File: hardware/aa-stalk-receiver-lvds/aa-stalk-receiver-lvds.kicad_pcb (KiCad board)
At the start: 2 copper layers, 67.3 x 50.8 mm, 81 parts, among them CN1 Conn_01x02, CN10 Conn_01x03, CN2 Conn_01x04, CN3 6P6C, CN4 Conn_01x03, CN5 Conn_01x02, CN6 Conn_01x02, CN7 Conn_01x02, CN8 Conn_01x02, CN9 Conn_01x03, Q1 KST10, Q2 MCH3484, Q3 MCH3484, U1 AZ1117-5.0, U2 MIC5504-3.3YM5, U3 LM4562, U4 FIN1028, U5 MC3486N

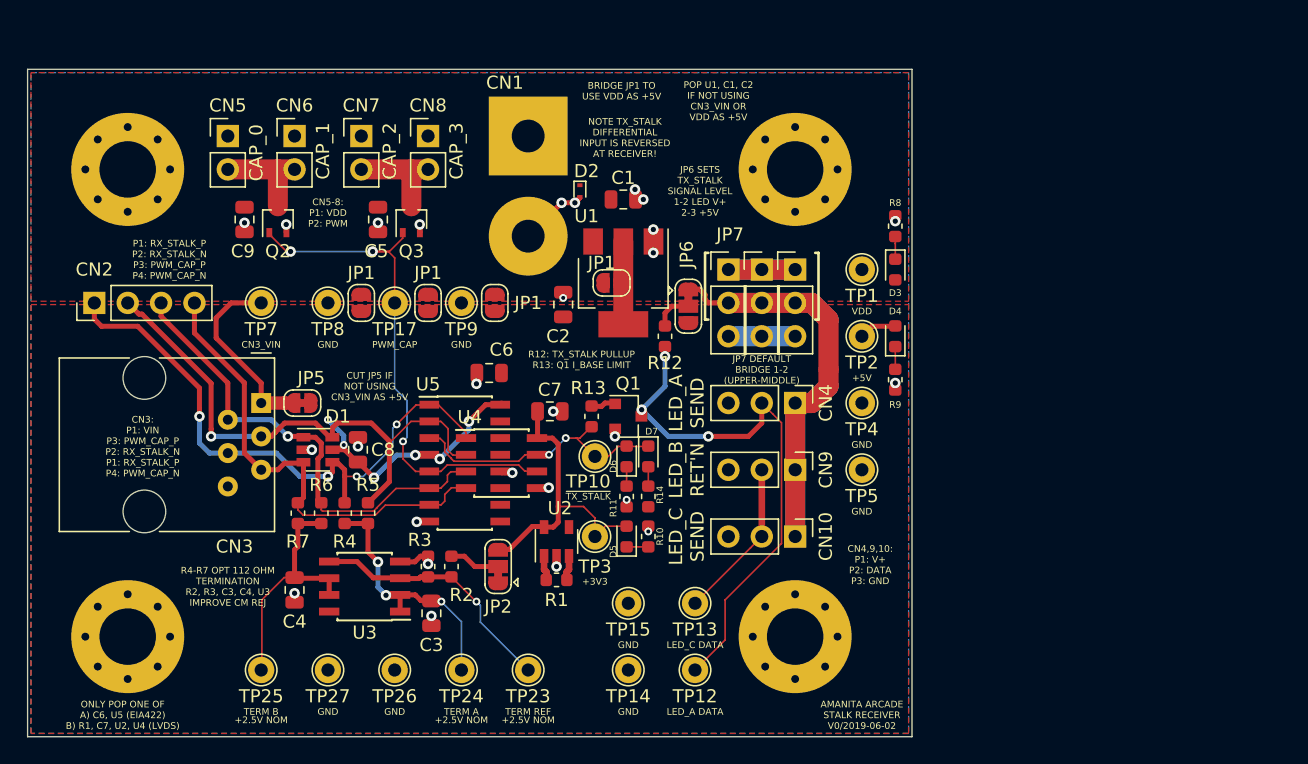
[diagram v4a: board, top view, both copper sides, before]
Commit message: Substantial rework of system, new layouts done for daughterboard, power, stalk receiver
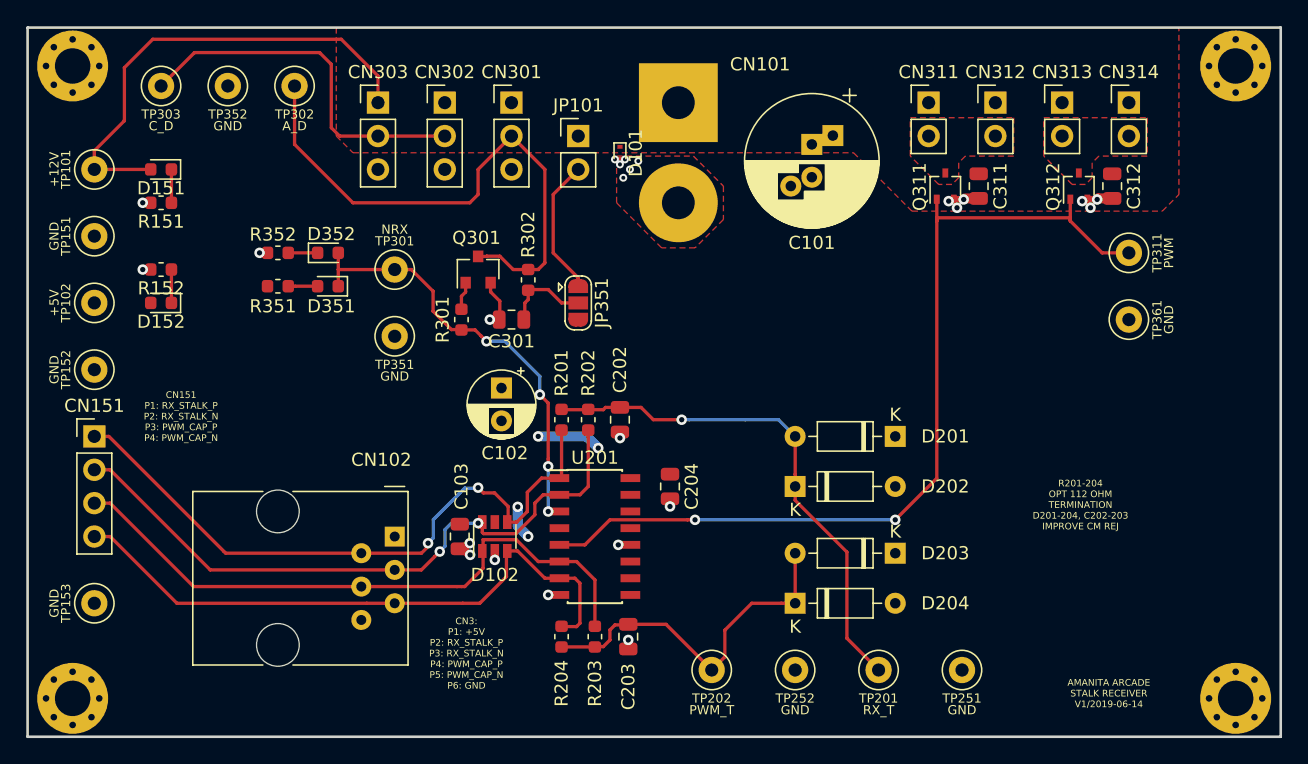
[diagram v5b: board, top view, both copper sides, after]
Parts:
- removed C1, C2, C5, C9: 10u, Capacitor_SMD:C_0805_2012Metric
- removed C3, C4, C7: 0.1u, Capacitor_SMD:C_0805_2012Metric
- removed C6, C8: 1u, Capacitor_SMD:C_0805_2012Metric
- removed CN1: Conn_01x02, Connector_Wire:SolderWirePad_1x02_P7.62mm_Drill2.5mm
- removed CN10, CN4, CN9: Conn_01x03, Connector_PinHeader_2.54mm:PinHeader_1x03_P2.54mm_Vertical
- removed CN2: Conn_01x04, Connector_PinHeader_2.54mm:PinHeader_1x04_P2.54mm_Vertical
- removed CN3: 6P6C, aa-shared:6P6C_Assmann_A-2014-1-4
- removed CN5, CN6, CN7, CN8: Conn_01x02, Connector_PinHeader_2.54mm:PinHeader_1x02_P2.54mm_Vertical
- removed D1: D5V0P4UR6SO, Package_TO_SOT_SMD:SOT-23-6
- removed D2: D_Zener, aa-shared:D_SOD-923
- removed D3, D4, D5, D6, D7: LED, Diode_SMD:D_0603_1608Metric
- removed JP1 (x4): SolderJumper_2_Open, Jumper:SolderJumper-2_P1.3mm_Open_RoundedPad1.0x1.5mm
- removed JP2, JP6: SolderJumper_3_Bridged12, Jumper:SolderJumper-3_P1.3mm_Bridged12_RoundedPad1.0x1.5mm
- removed JP5: SolderJumper_2_Bridged, Jumper:SolderJumper-2_P1.3mm_Bridged_RoundedPad1.0x1.5mm
- removed JP7 (x3): Jumper_3_Bridged12, Connector_PinHeader_2.54mm:PinHeader_1x03_P2.54mm_Vertical
- removed Q1: KST10, Package_TO_SOT_SMD:SOT-23
- removed Q2, Q3: MCH3484, Package_TO_SOT_SMD:SOT-323_SC-70
- removed R1, R2, R3: 10k, Resistor_SMD:R_0603_1608Metric
- removed R10: 220, Resistor_SMD:R_0603_1608Metric
- removed R11, R14, R9: 470, Resistor_SMD:R_0603_1608Metric
- removed R12, R13: 1k, Resistor_SMD:R_0603_1608Metric
- removed R4, R5, R6, R7: 56, Resistor_SMD:R_0603_1608Metric
- removed R8: 1.5k, Resistor_SMD:R_0603_1608Metric
- removed TP1, TP10, TP12, TP13, TP14, TP15, TP17, TP2, TP23, TP24, TP25, TP26, TP27, TP3, TP4, TP5, TP7, TP8, TP9: TestPoint, TestPoint:TestPoint_THTPad_D2.0mm_Drill1.0mm
- removed U1: AZ1117-5.0, Package_TO_SOT_SMD:SOT-223-3_TabPin2
- removed U2: MIC5504-3.3YM5, Package_TO_SOT_SMD:SOT-23-5
- removed U3: LM4562, Package_SO:SOIC-8_3.9x4.9mm_P1.27mm
- removed U4: FIN1028, Package_SO:SOIC-8_3.9x4.9mm_P1.27mm
- removed U5: MC3486N, Package_SO:SOIC-16_3.9x9.9mm_P1.27mm
- added C101: 100u, Capacitor_THT:CP_Radial_D10.0mm_P2.50mm_P5.00mm, F.Cu at (151.1, 59.1)
- added C102: 10u, Capacitor_THT:CP_Radial_D5.0mm_P2.50mm, F.Cu at (127.5, 77.6)
- added C103: 1u, Capacitor_SMD:C_0805_2012Metric, F.Cu at (124.3, 88.9)
- added C202: 0.1u, Capacitor_SMD:C_0805_2012Metric, F.Cu at (136.5, 80.0)
- added C203: 0.1u, Capacitor_SMD:C_0805_2012Metric, F.Cu at (137.2, 96.5)
- added C204: 1u, Capacitor_SMD:C_0805_2012Metric, F.Cu at (140.3, 85.1)
- added C301: 0.1u, Capacitor_SMD:C_0805_2012Metric, F.Cu at (128.3, 72.4)
- added C311: 10u, Capacitor_SMD:C_0805_2012Metric, F.Cu at (163.8, 62.2)
- added C312: 10u, Capacitor_SMD:C_0805_2012Metric, F.Cu at (174.0, 62.2)
- added CN101: Conn_01x02, Connector_Wire:SolderWirePad_1x02_P7.62mm_Drill2.5mm, F.Cu at (141.0, 55.9)
- added CN102: 6P6C, aa-shared:6P6C_Assmann_A-2014-1-4, F.Cu at (119.4, 88.9)
- added CN151: Conn_01x04, Connector_PinHeader_2.54mm:PinHeader_1x04_P2.54mm_Vertical, F.Cu at (96.5, 81.3)
- added CN301: Conn_01x03, Connector_PinHeader_2.54mm:PinHeader_1x03_P2.54mm_Vertical, F.Cu at (128.3, 55.9)
- added CN302: Conn_01x03, Connector_PinHeader_2.54mm:PinHeader_1x03_P2.54mm_Vertical, F.Cu at (123.2, 55.9)
- added CN303: Conn_01x03, Connector_PinHeader_2.54mm:PinHeader_1x03_P2.54mm_Vertical, F.Cu at (118.1, 55.9)
- added CN311: Conn_01x02, Connector_PinHeader_2.54mm:PinHeader_1x02_P2.54mm_Vertical, F.Cu at (160.0, 55.9)
- added CN312: Conn_01x02, Connector_PinHeader_2.54mm:PinHeader_1x02_P2.54mm_Vertical, F.Cu at (165.1, 55.9)
- added CN313: Conn_01x02, Connector_PinHeader_2.54mm:PinHeader_1x02_P2.54mm_Vertical, F.Cu at (170.2, 55.9)
- added CN314: Conn_01x02, Connector_PinHeader_2.54mm:PinHeader_1x02_P2.54mm_Vertical, F.Cu at (175.3, 55.9)
- added D101: D_Zener, aa-shared:D_SOD-923, F.Cu at (136.5, 59.7)
- added D102: D5V0P4UR6SO, Package_TO_SOT_SMD:SOT-23-6, F.Cu at (127.0, 88.9)
- added D151: LED, Diode_SMD:D_0603_1608Metric, F.Cu at (101.6, 61.0)
- added D152: LED, Diode_SMD:D_0603_1608Metric, F.Cu at (101.6, 71.1)
- added D201: BZX79C2V7, Diode_THT:D_DO-35_SOD27_P7.62mm_Horizontal, F.Cu at (157.5, 81.3)
- added D202: BZX79C2V7, Diode_THT:D_DO-35_SOD27_P7.62mm_Horizontal, F.Cu at (149.9, 85.1)
- added D203: BZX79C2V7, Diode_THT:D_DO-35_SOD27_P7.62mm_Horizontal, F.Cu at (157.5, 90.2)
- added D204: BZX79C2V7, Diode_THT:D_DO-35_SOD27_P7.62mm_Horizontal, F.Cu at (149.9, 94.0)
- added D351: LED, Diode_SMD:D_0603_1608Metric, F.Cu at (114.3, 69.8)
- added D352: LED, Diode_SMD:D_0603_1608Metric, F.Cu at (114.3, 67.3)
- added JP101: Jumper_2_Bridged, Connector_PinHeader_2.54mm:PinHeader_1x02_P2.54mm_Vertical, F.Cu at (133.3, 58.4)
- added JP351: SolderJumper_3_Bridged12, Jumper:SolderJumper-3_P1.3mm_Open_RoundedPad1.0x1.5mm, F.Cu at (133.3, 71.1)
- added Q301: KST10, Package_TO_SOT_SMD:SOT-23, F.Cu at (125.7, 68.6)
- added Q311: MCH3484, Package_TO_SOT_SMD:SOT-323_SC-70, F.Cu at (161.3, 62.2)
- added Q312: MCH3484, Package_TO_SOT_SMD:SOT-323_SC-70, F.Cu at (171.4, 62.2)
- added R151: 1.5k, Resistor_SMD:R_0603_1608Metric, F.Cu at (101.6, 63.5)
- added R152: 470, Resistor_SMD:R_0603_1608Metric, F.Cu at (101.6, 68.6)
- added R201: 56, Resistor_SMD:R_0603_1608Metric, F.Cu at (132.1, 80.0)
- added R202: 56, Resistor_SMD:R_0603_1608Metric, F.Cu at (134.1, 80.0)
- added R203: 56, Resistor_SMD:R_0603_1608Metric, F.Cu at (134.6, 96.5)
- added R204: 56, Resistor_SMD:R_0603_1608Metric, F.Cu at (132.1, 96.5)
- added R301: 1k, Resistor_SMD:R_0603_1608Metric, F.Cu at (124.5, 72.4)
- added R302: 1k, Resistor_SMD:R_0603_1608Metric, F.Cu at (129.5, 69.4)
- added R351: 470, Resistor_SMD:R_0603_1608Metric, F.Cu at (110.5, 69.8)
- added R352: 470, Resistor_SMD:R_0603_1608Metric, F.Cu at (110.5, 67.3)
- added TP101: +12V, aa-shared:TestPoint_Loop_D1.80mm_Drill1.0mm_Beaded, F.Cu at (96.5, 61.0)
- added TP102: +5V, aa-shared:TestPoint_Loop_D1.80mm_Drill1.0mm_Beaded, F.Cu at (96.5, 71.1)
- added TP151: GND, aa-shared:TestPoint_Loop_D1.80mm_Drill1.0mm_Beaded, F.Cu at (96.5, 66.0)
- added TP152: GND, aa-shared:TestPoint_Loop_D1.80mm_Drill1.0mm_Beaded, F.Cu at (96.5, 76.2)
- added TP153: GND, aa-shared:TestPoint_Loop_D1.80mm_Drill1.0mm_Beaded, F.Cu at (96.5, 94.0)
- added TP201: RX_T, aa-shared:TestPoint_Loop_D1.80mm_Drill1.0mm_Beaded, F.Cu at (156.2, 99.1)
- added TP202: PWM_T, aa-shared:TestPoint_Loop_D1.80mm_Drill1.0mm_Beaded, F.Cu at (143.5, 99.1)
- added TP251: GND, aa-shared:TestPoint_Loop_D1.80mm_Drill1.0mm_Beaded, F.Cu at (162.6, 99.1)
- added TP252: GND, aa-shared:TestPoint_Loop_D1.80mm_Drill1.0mm_Beaded, F.Cu at (149.9, 99.1)
- added TP301: NRX, aa-shared:TestPoint_Loop_D1.80mm_Drill1.0mm_Beaded, F.Cu at (119.4, 68.6)
- added TP302: A_D, aa-shared:TestPoint_Loop_D1.80mm_Drill1.0mm_Beaded, F.Cu at (111.8, 54.6)
- added TP303: C_D, aa-shared:TestPoint_Loop_D1.80mm_Drill1.0mm_Beaded, F.Cu at (101.6, 54.6)
- added TP311: PWM, aa-shared:TestPoint_Loop_D1.80mm_Drill1.0mm_Beaded, F.Cu at (175.3, 67.3)
- added TP351: GND, aa-shared:TestPoint_Loop_D1.80mm_Drill1.0mm_Beaded, F.Cu at (119.4, 73.7)
- added TP352: GND, aa-shared:TestPoint_Loop_D1.80mm_Drill1.0mm_Beaded, F.Cu at (106.7, 54.6)
- added TP361: GND, aa-shared:TestPoint_Loop_D1.80mm_Drill1.0mm_Beaded, F.Cu at (175.3, 72.4)
- added U201: ST26C32, Package_SO:SOIC-16_3.9x9.9mm_P1.27mm, F.Cu at (134.6, 88.9)
- H1, H2, H3, H4: footprint MountingHole:MountingHole_4.3mm_M4_Pad_Via -> MountingHole:MountingHole_2.7mm_M2.5_Pad_Via
- moved H2 94.9 mm to (183.4, 53.1)
- moved H3 68.2 mm to (94.9, 101.2)
- moved H4 33.9 mm to (183.4, 101.2)
- moved H1 8.92 mm to (94.9, 53.1)
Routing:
- net /LED_POWER: track 56.7 -> 0.00 mm
- net Net-(C202-Pad1): track 0.00 -> 39.3 mm, vias 0 -> 1
- net /VIN: track 0.00 -> 36.4 mm
- net /N_RX_STALK: track 0.00 -> 33.6 mm, vias 0 -> 4
- net /PWM_CAP: track 40.4 -> 69.8 mm, vias 3 -> 2
- net +5V: track 36.9 -> 8.10 mm, vias 6 -> 4
- net /LED_C_DATA: track 0.00 -> 28.1 mm
- net Net-(C203-Pad1): track 0.00 -> 27.8 mm
- net +3V3: track 22.5 -> 0.00 mm
- net /RX_STALK: track 21.0 -> 0.00 mm, vias 2 -> 0
- net Net-(R2-Pad2): track 19.5 -> 0.00 mm, vias 1 -> 0
- net /+2.5A: track 19.1 -> 0.00 mm, vias 3 -> 0
- net /+2.5B: track 18.2 -> 0.00 mm
- net Net-(CN3-Pad1): track 14.3 -> 0.00 mm
- net Net-(CN10-Pad2): track 12.3 -> 0.00 mm
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- added copper zone on F.Cu, net /VIN
- added copper zone on F.Cu, net GND
- added copper zone on F.Cu, net Net-(CN311-Pad2)
- added copper zone on F.Cu, net Net-(CN313-Pad2)
- removed copper zone on F.Cu, net VDD
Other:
- board size 67.3 x 50.8 mm -> 95.4 x 54 mm
- net class Default: clearance 0.127 -> 0.2032; trace_width 0.381 -> 0.254
- net class High current: clearance 0.127 -> 0.254
- rule trace_clearance: 0.127 -> 0.2032
- board text added: "AMANITA ARCADE STALK RECEIVER V1/2019-06-14"
- board text added: "CN151 P1: RX_STALK_P P2: RX_STALK_N P3: PWM_CAP_P P4: PWM_CAP_N"
- board text added: "CN3: P1: +5V P2: RX_STALK_P P3: RX_STALK_N P4: PWM_CAP_P P5: PWM_CAP_N P6: GND"
- board text added: "PWM_CAP_N"
- board text added: "PWM_CAP_P"
- board text added: "R201-204 OPT 112 OHM TERMINATION D201-204, C202-203 IMPROVE CM REJ"
- board text added: "RX_STALK_N"
- board text added: "RX_STALK_P"
- board text removed: "+2.5V NOM"
- board text removed: "+3V3"
- board text removed: "+5V"
- board text removed: "AMANITA ARCADE STALK RECEIVER V0/2019-06-02"
- board text removed: "BRIDGE JP1 TO USE VDD AS +5V"
- board text removed: "CAP_0"
- board text removed: "CAP_1"
- board text removed: "CAP_2"
- board text removed: "CAP_3"
- board text removed: "CN3: P1: VIN P3: PWM_CAP_P P2: RX_STALK_N P1: RX_STALK_P P4: PWM_CAP_N"
- board text removed: "CN3_VIN"
- board text removed: "CN4,9,10: P1: V+ P2: DATA P3: GND"
- board text removed: "CN5-8: P1: VDD P2: PWM"
- board text removed: "CUT JP5 IF NOT USING CN3_VIN AS +5V"
- board text removed: "GND"
- board text removed: "JP6 SETS TX_STALK SIGNAL LEVEL 1-2 LED V+ 2-3 +5V"
- board text removed: "JP7 DEFAULT BRIDGE 1-2 (UPPER-MIDDLE)"
- board text removed: "LED_A DATA"
- board text removed: "LED_A SEND"
- board text removed: "LED_B RET'N"
- board text removed: "LED_C DATA"
- board text removed: "LED_C SEND"
- board text removed: "NOTE TX_STALK DIFFERENTIAL INPUT IS REVERSED AT RECEIVER!"
- board text removed: "ONLY POP ONE OF A) C6, U5 (EIA422) B) R1, C7, U2, U4 (LVDS)"
- board text removed: "P1: RX_STALK_P P2: RX_STALK_N P3: PWM_CAP_P P4: PWM_CAP_N"
- board text removed: "POP U1, C1, C2 IF NOT USING CN3_VIN OR VDD AS +5V"
- board text removed: "PWM_CAP"
- board text removed: "R12: TX_STALK PULLUP R13: Q1 I_BASE LIMIT"
- board text removed: "R4-R7 OPT 112 OHM TERMINATION R2, R3, C3, C4, U3 IMPROVE CM REJ"
- board text removed: "TERM A"
- board text removed: "TERM B"
- board text removed: "TERM REF"
- board text removed: "VDD"
- board text removed: "~TX_STALK"

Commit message: Final designs and actual sent gerbers for first for-real run
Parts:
- added FD1: Fiducial, Fiducial:Fiducial_1mm_Dia_2.54mm_Outer_CopperTop, F.Cu at (97.8, 97.8)
- added FD2: Fiducial, Fiducial:Fiducial_1mm_Dia_2.54mm_Outer_CopperTop, F.Cu at (181.6, 58.4)
- added FD5: Fiducial, aa-shared:StencilAlignment_1.27mm, F.Cu at (94.0, 96.5)
- added FD6: Fiducial, aa-shared:StencilAlignment_1.27mm, F.Cu at (184.2, 58.4)
- D101: value D_Zener -> DF2S16FS
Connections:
- C301 pad 1: Net-(C301-Pad1) -> +12V
- JP351 pad 2: Net-(C301-Pad1) -> +12V
- R302 pad 1: Net-(C301-Pad1) -> +12V
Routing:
- net +12V: track 10.5 -> 18.3 mm
- net Net-(C301-Pad1): track 6.57 -> 0.00 mm
- net /LED_A_DATA: track 42.4 -> 38.2 mm

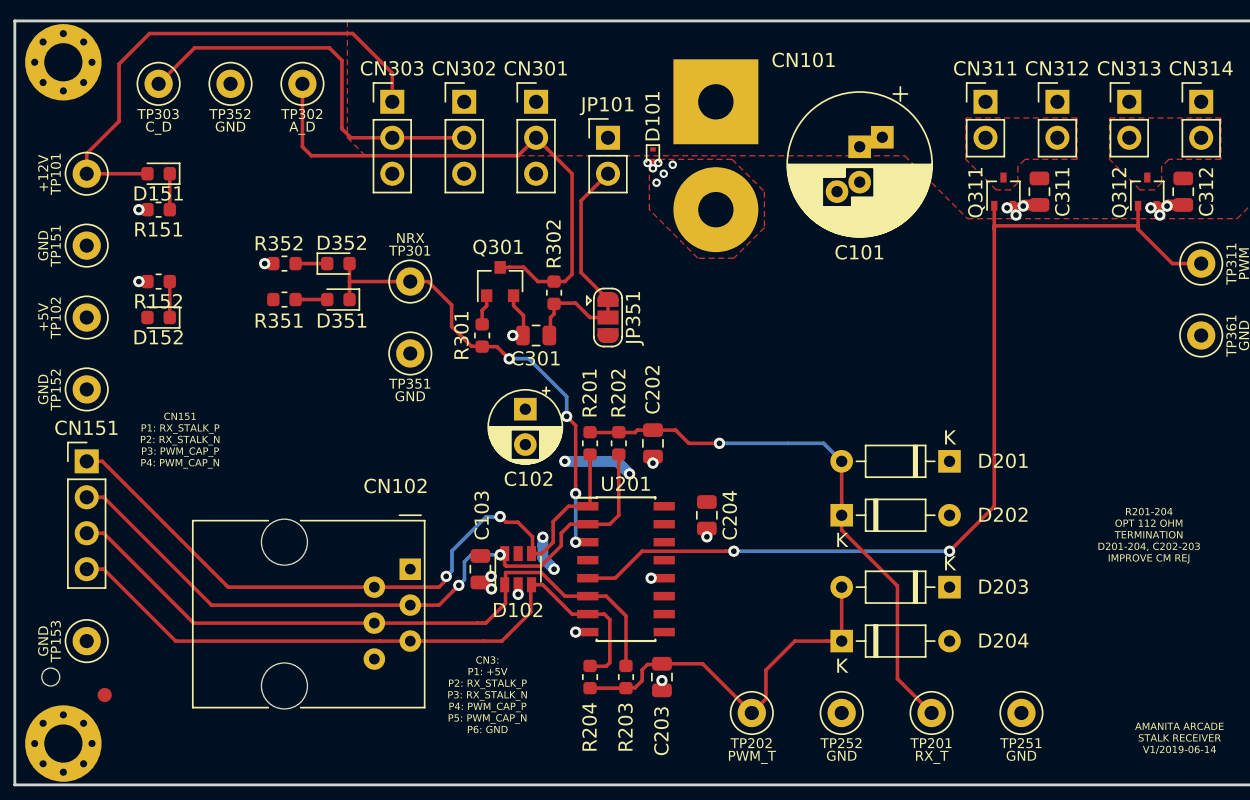
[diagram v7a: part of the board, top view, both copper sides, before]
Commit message: Minor board updates to fix issues discovered during build
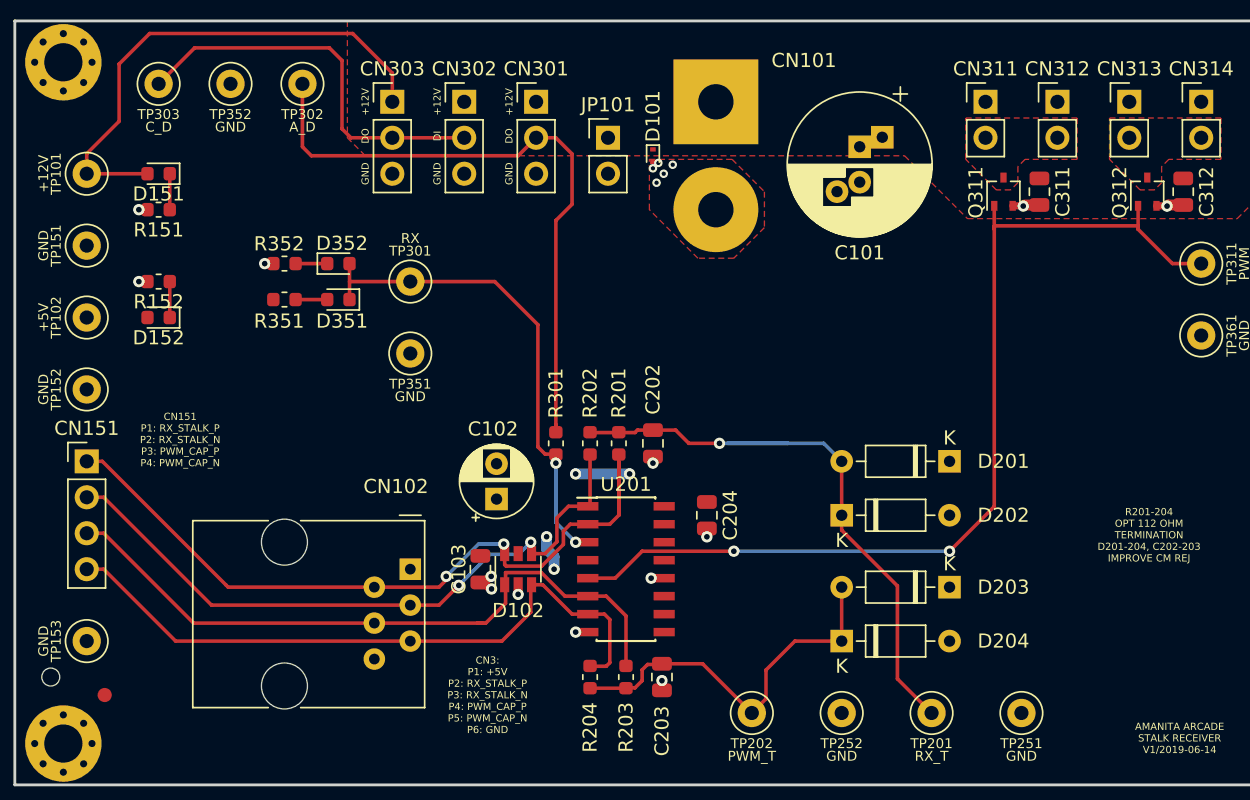
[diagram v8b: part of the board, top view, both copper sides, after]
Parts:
- removed C301: 0.1u, Capacitor_SMD:C_0805_2012Metric
- removed JP351: SolderJumper_3_Bridged12, Jumper:SolderJumper-3_P1.3mm_Open_RoundedPad1.0x1.5mm
- removed Q301: KST10, Package_TO_SOT_SMD:SOT-23
- removed R302: 1k, Resistor_SMD:R_0603_1608Metric
- D102: value D5V0P4UR6SO -> DS1042
- R301: value 1k -> 120
- TP301: value NRX -> RX
- moved R301 9.23 mm to (129.7, 80.0)
- moved C102 6.67 mm to (125.5, 83.9), turned to 90 degrees
- moved R201 2.03 mm to (134.1, 80.0)
- moved R202 2.03 mm to (132.1, 80.0)
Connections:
- net /N_RX_STALK renamed /RX_STALK
- D102 pad 4: /RX_STALK_P -> /RX_STALK_N
- D102 pad 6: /RX_STALK_N -> /RX_STALK_P
- R301 pad 2: Net-(Q301-Pad1) -> /LED_A_DATA
- U201 pad 1: /RX_STALK_P -> /RX_STALK_N
- U201 pad 2: /RX_STALK_N -> /RX_STALK_P
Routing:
- net +12V: track 18.3 -> 0.00 mm
- net /LED_A_DATA: track 38.2 -> 44.9 mm
- net /RX_STALK_P: track 49.8 -> 54.1 mm
- net Net-(C202-Pad1): track 39.3 -> 43.6 mm
- net GND: track 15.5 -> 11.8 mm, vias 24 -> 18
- net /RX_STALK_N: track 50.2 -> 47.2 mm
- net Net-(Q301-Pad1): track 2.18 -> 0.00 mm
- net /RX_STALK: track 33.6 -> 34.9 mm, vias 4 -> 2
- net +5V: track 8.10 -> 6.90 mm
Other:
- board text added: "+12V"
- board text added: "DI"
- board text added: "DO"
- board text added: "GND"
